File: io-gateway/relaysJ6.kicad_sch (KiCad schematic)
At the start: 24 parts, among them K1 2071556-2, K2 2071556-2, K3 2071556-2, K4 2071556-2, K5 2071556-2, K6 2071556-2, Q1 NTR4003NT1G, Q2 NTR4003NT1G, Q3 NTR4003NT1G, Q4 NTR4003NT1G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

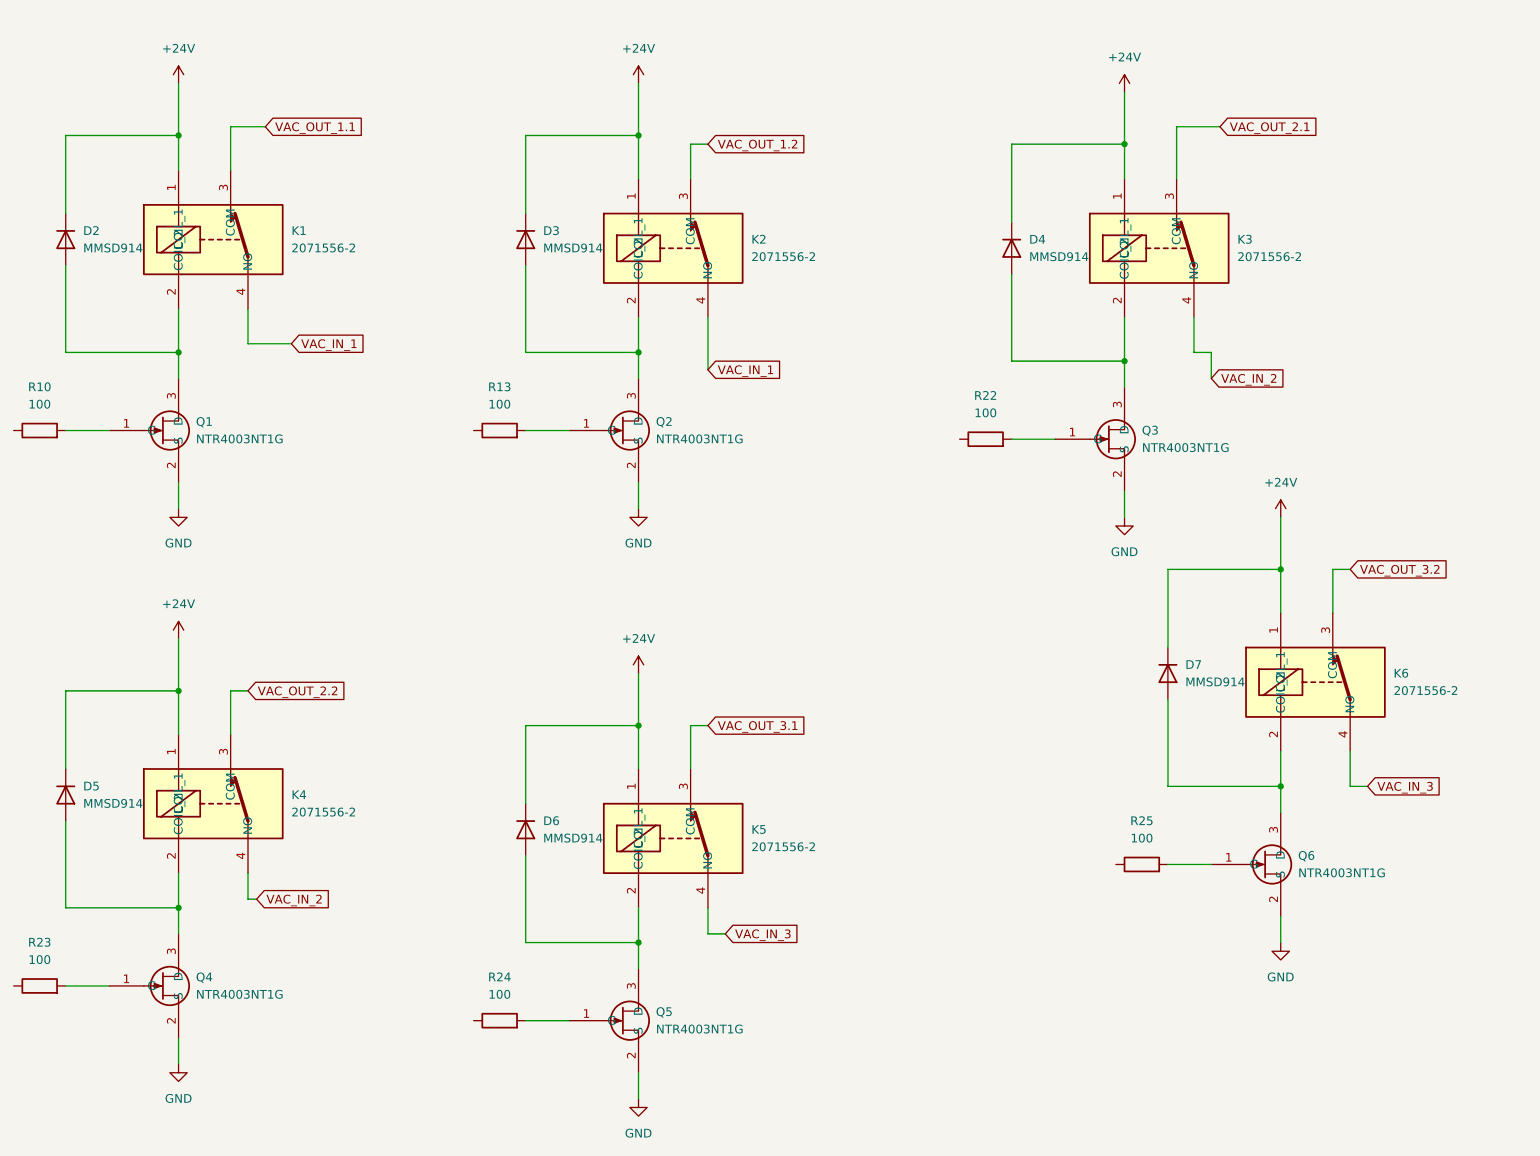
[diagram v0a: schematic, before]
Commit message: Place Relays
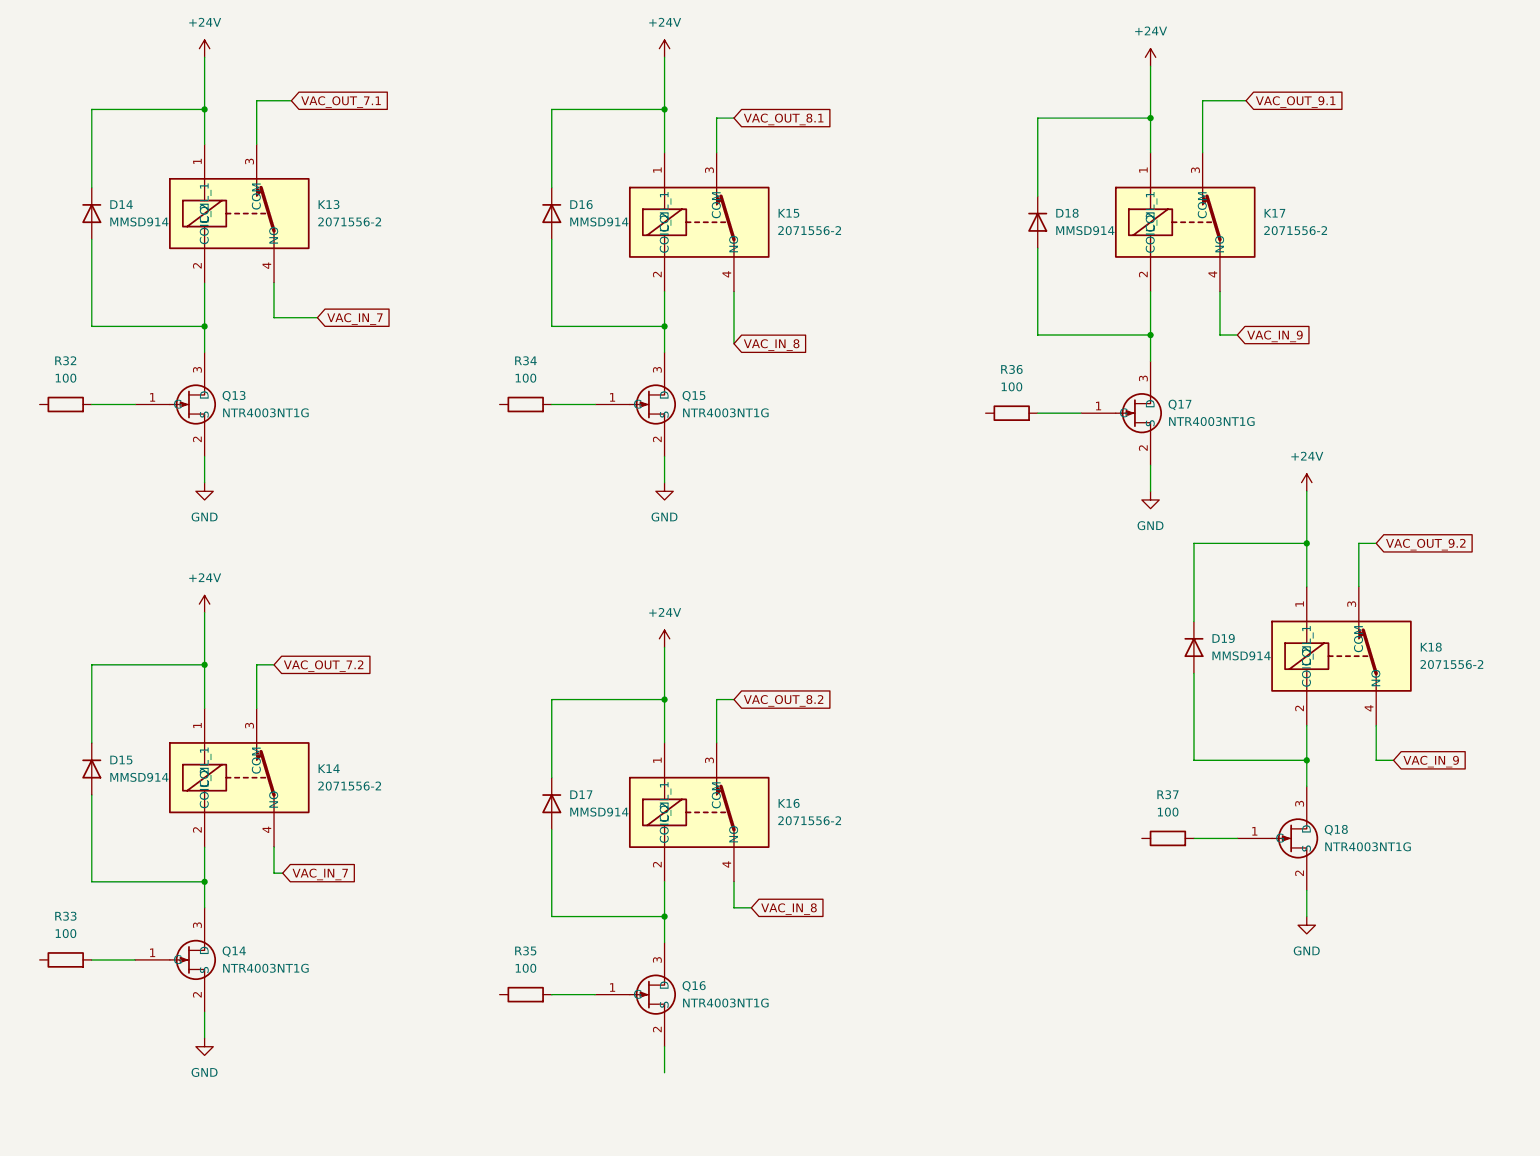
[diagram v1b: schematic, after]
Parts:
- removed D2, D3, D4, D5, D6, D7: MMSD914, Diode_SMD:D_SOD-123, symbol Diode:MMSD914
- removed K1, K2, K3, K4, K5, K6: 2071556-2, 20715562, symbol 2071556-2:2071556-2
- removed Q1, Q2, Q3, Q4, Q5, Q6: NTR4003NT1G, Package_TO_SOT_SMD:SOT-23-3, symbol NTR4003NT1G:NTR4003NT1G
- removed R10, R13, R22, R23, R24, R25: 100, Resistor_SMD:R_0603_1608Metric, symbol Device:R
- added D14, D15, D16, D17, D18, D19: MMSD914, Diode_SMD:D_SOD-123, symbol Diode:MMSD914
- added K13, K14, K15, K16, K17, K18: 2071556-2, 20715562, symbol 2071556-2:2071556-2
- added Q13, Q14, Q15, Q16, Q17, Q18: NTR4003NT1G, Package_TO_SOT_SMD:SOT-23-3, symbol NTR4003NT1G:NTR4003NT1G
- added R32, R33, R34, R35, R36, R37: 100, Resistor_SMD:R_0603_1608Metric, symbol Device:R
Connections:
- net +24V: now also D14.1 (K), D15.1 (K), D16.1 (K), D17.1 (K), D18.1 (K), D19.1 (K), K13.1 (COIL_1), K14.1 (COIL_1), K15.1 (COIL_1), K16.1 (COIL_1), K17.1 (COIL_1), K18.1 (COIL_1)
- net GND: now also Q13.2 (S), Q14.2 (S), Q15.2 (S), Q17.2 (S), Q18.2 (S)
- new net: D17.2 (A), K16.2 (COIL_2), Q16.3 (D)
- new net: Q15.1 (G), R34.2
- new net: D19.2 (A), K18.2 (COIL_2), Q18.3 (D)
- new net: D16.2 (A), K15.2 (COIL_2), Q15.3 (D)
- new net: D15.2 (A), K14.2 (COIL_2), Q14.3 (D)
- new net: Q16.1 (G), R35.2
- new net: Q17.1 (G), R36.2
- new net: D14.2 (A), K13.2 (COIL_2), Q13.3 (D)
- new net: Q18.1 (G), R37.2
- new net: Q13.1 (G), R32.2
- new net: Q14.1 (G), R33.2
- new net: D18.2 (A), K17.2 (COIL_2), Q17.3 (D)
- new net VAC_IN_7: K13.4 (NO), K14.4 (NO)
- new net VAC_IN_8: K15.4 (NO), K16.4 (NO)
- new net VAC_IN_9: K17.4 (NO), K18.4 (NO)
- new net VAC_OUT_7.1: K13.3 (COM)
- new net VAC_OUT_7.2: K14.3 (COM)
- new net VAC_OUT_8.1: K15.3 (COM)
- new net VAC_OUT_8.2: K16.3 (COM)
- new net VAC_OUT_9.1: K17.3 (COM)
- new net VAC_OUT_9.2: K18.3 (COM)

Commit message: update
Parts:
- removed D14, D15, D16, D17, D18, D19: MMSD914, Diode_SMD:D_SOD-123, symbol Diode:MMSD914
- removed K13, K14, K15, K16, K17, K18: 2071556-2, 20715562, symbol 2071556-2:2071556-2
- removed Q13, Q14, Q15, Q16, Q17, Q18: NTR4003NT1G, Package_TO_SOT_SMD:SOT-23-3, symbol NTR4003NT1G:NTR4003NT1G
- removed R32, R33, R34, R35, R36, R37: 100, Resistor_SMD:R_0603_1608Metric, symbol Device:R

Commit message: add RS485
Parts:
- added C1, C3: 100nF, Capacitor_SMD:C_0603_1608Metric, symbol Device:C
- added C2, C4: 10µF, Capacitor_SMD:C_0603_1608Metric, symbol Device:C
- added C5: 100µF, Capacitor_SMD:C_0603_1608Metric, symbol Device:C
- added D2, D3: MBR0520, Diode_SMD:D_SOD-123, symbol Diode:MBR0520
- added R1, R2: 4k7, Resistor_SMD:R_0201_0603Metric, symbol Device:R
- added TR1: Wuerth_750315371, Transformer_SMD:Transformer_Wuerth_750315371, symbol Transformer:Wuerth_750315371
- added U1: SN65LBC176QDR, Package_SO:SOIC-8_3.9x4.9mm_P1.27mm, symbol Interface_UART:SN65LBC176QDR
- added U2: TPS76350, Package_TO_SOT_SMD:SOT-23-5, symbol Regulator_Linear:TPS76350
- added U4: ISO7741, Package_SO:SOIC-16W_7.5x10.3mm_P1.27mm, symbol DigitalIsolator:ISO7741
- added U5: SN6501DBVR, Package_TO_SOT_SMD:SOT-23-5, symbol PowerManagement:SN6501DBVR
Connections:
- new net: R2.2, U4.7 (EN1)
- new net: TR1.1, U5.3 (D2)
- new net: TR1.3, U5.1 (D1)
- new net: C4.1, C5.1, D2.1 (K), TR1.4, U2.1 (VIN), U2.3 (EN)
- new net: D3.2 (A), TR1.5
- new net: D2.2 (A), TR1.6
- new net: U1.1 (R), U4.11 (IND)
- new net: U1.2 (~{RE}), U4.12 (OUTC)
- new net: U1.3 (DE), U4.14 (OUTA)
- new net: U1.4 (D), U4.13 (OUTB)
- new net: C4.2, C5.2, D3.1 (K)
- new net: C2.1, C3.1, R1.1, U2.5 (VOUT), U4.16 (VCC2)
- new net: R1.2, U4.10 (EN2)
- new net +5V: C1.1, R2.1, TR1.2, U1.8 (VCC), U4.1 (VCC1), U5.2 (VCC)
- new net GND: C1.2, U4.2 (GND1), U4.8 (GND1), U5.4 (GND), U5.5 (GND)
- new net GND2: C2.2, C3.2, U1.5 (GND), U2.2 (GND), U4.15 (GND2), U4.9 (GND2)
- new net RS485_DIR: U4.4 (INB)
- new net RS485_RxD: U4.6 (OUTD)
- new net RS485__TXD: U4.5 (INC)

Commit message: upd rs485
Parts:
- C5: value 100µF -> 100nF
- R1, R2: footprint Resistor_SMD:R_0201_0603Metric -> Resistor_SMD:R_0603_1608Metric
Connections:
- net GND2: now also C4.2, C5.2, D3.1 (K)
- net at U1.2 (~{RE}): now also U4.14 (OUTA); no longer U4.12 (OUTC)
- net at U1.3 (DE): now also U4.13 (OUTB); no longer U4.14 (OUTA)
- net at U1.4 (D): now also U4.12 (OUTC); no longer U4.13 (OUTB)
- net RS485_A: now reaches U1.6 (A)
- net RS485_B: now reaches U1.7 (B)
- net RS485_DIR renamed RS485_RTS
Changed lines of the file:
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@@
+	)
+	(junction
+		(at 123.19 87.63)
+		(diameter 0)
+		(color 0 0 0 0)
 	)
 	(junction
@@
 		(color 0 0 0 0)
 	)
+	(junction
+		(at 140.97 87.63)
+		(diameter 0)
+		(color 0 0 0 0)
+	)
+	(wire
+		(pts
+			(xy 123.19 87.63) (xy 140.97 87.63)
+		)
+		(stroke
+			(width 0)
+			(type default)
+		)
+	)
 	(wire
 		(pts
@@
 	(wire
 		(pts
-			(xy 196.85 113.03) (xy 196.85 115.57)
-		)
-		(stroke
-			(width 0)
-			(type default)
-		)
-	)
-	(wire
-		(pts
 			(xy 148.59 76.2) (xy 154.94 76.2)
 		)
@@
 	(wire
 		(pts
+			(xy 196.85 115.57) (xy 196.85 110.49)
+		)
+		(stroke
+			(width 0)
+			(type default)
+		)
+	)
+	(wire
+		(pts
 			(xy 91.44 81.28) (xy 91.44 87.63)
 		)
@@
 	(wire
 		(pts
+			(xy 190.5 118.11) (xy 198.12 118.11)
+		)
+		(stroke
+			(width 0)
+			(type default)
+		)
+	)
+	(wire
+		(pts
 			(xy 166.37 100.33) (xy 166.37 96.52)
 		)
@@
 	(wire
 		(pts
+			(xy 200.66 114.3) (xy 200.66 118.11)
+		)
+		(stroke
+			(width 0)
+			(type default)
+		)
+	)
+	(wire
+		(pts
 			(xy 193.04 100.33) (xy 195.58 100.33)
 		)
@@
 	(wire
 		(pts
-			(xy 196.85 115.57) (xy 190.5 115.57)
-		)
-		(stroke
-			(width 0)
-			(type default)
-		)
-	)
-	(wire
-		(pts
 			(xy 45.72 76.2) (xy 45.72 86.36)
 		)
@@
 	(wire
 		(pts
+			(xy 140.97 88.9) (xy 140.97 87.63)
+		)
+		(stroke
+			(width 0)
+			(type default)
+		)
+	)
+	(wire
+		(pts
 			(xy 73.66 78.74) (xy 67.31 78.74)
 		)
@@
 	(wire
 		(pts
-			(xy 193.04 113.03) (xy 190.5 113.03)
+			(xy 196.85 110.49) (xy 201.93 110.49)
+		)
+		(stroke
+			(width 0)
+			(type default)
+		)
+	)
+	(wire
+		(pts
+			(xy 190.5 113.03) (xy 194.31 113.03)
 		)
 		(stroke
@@
 	(wire
 		(pts
-			(xy 135.89 86.36) (xy 140.97 86.36)
+			(xy 217.17 120.65) (xy 224.79 120.65)
 		)
 		(stroke
@@
 	(wire
 		(pts
+			(xy 217.17 118.11) (xy 224.79 118.11)
+		)
+		(stroke
+			(width 0)
+			(type default)
+		)
+	)
+	(wire
+		(pts
 			(xy 190.5 76.2) (xy 167.64 76.2)
 		)
@@
 	(wire
 		(pts
+			(xy 198.12 118.11) (xy 198.12 113.03)
+		)
+		(stroke
+			(width 0)
+			(type default)
+		)
+	)
+	(wire
+		(pts
 			(xy 110.49 87.63) (xy 110.49 85.09)
 		)
@@
 	(wire
 		(pts
-			(xy 193.04 110.49) (xy 193.04 113.03)
-		)
-		(stroke
-			(width 0)
-			(type default)
-		)
-	)
-	(wire
-		(pts
 			(xy 73.66 83.82) (xy 67.31 83.82)
 		)
@@
 	(wire
 		(pts
+			(xy 198.12 113.03) (xy 201.93 113.03)
+		)
+		(stroke
+			(width 0)
+			(type default)
+		)
+	)
+	(wire
+		(pts
 			(xy 67.31 78.74) (xy 67.31 76.2)
 		)
@@
 	(wire
 		(pts
-			(xy 190.5 118.11) (xy 201.93 118.11)
+			(xy 194.31 113.03) (xy 194.31 114.3)
 		)
 		(stroke
@@
 	(wire
 		(pts
+			(xy 190.5 115.57) (xy 196.85 115.57)
+		)
+		(stroke
+			(width 0)
+			(type default)
+		)
+	)
+	(wire
+		(pts
+			(xy 200.66 118.11) (xy 201.93 118.11)
+		)
+		(stroke
+			(width 0)
+			(type default)
+		)
+	)
+	(wire
+		(pts
 			(xy 101.6 76.2) (xy 101.6 83.82)
 		)
@@
 	(wire
 		(pts
-			(xy 201.93 110.49) (xy 193.04 110.49)
-		)
-		(stroke
-			(width 0)
-			(type default)
-		)
-	)
-	(wire
-		(pts
 			(xy 123.19 76.2) (xy 130.81 76.2)
 		)
@@
 	(wire
 		(pts
+			(xy 194.31 114.3) (xy 200.66 114.3)
+		)
+		(stroke
+			(width 0)
+			(type default)
+		)
+	)
+	(wire
+		(pts
 			(xy 67.31 86.36) (xy 64.77 86.36)
 		)
@@
 	(wire
 		(pts
-			(xy 201.93 113.03) (xy 196.85 113.03)
+			(xy 140.97 87.63) (xy 140.97 86.36)
 		)
 		(stroke
@@
 		)
 	)
-	(hierarchical_label "RS485_DIR"
+	(hierarchical_label "RS485_B"
+		(shape bidirectional)
+		(at 224.79 118.11 0)
+		(effects
+			(font
+				(size 1.27 1.27)
+			)
+			(justify left)
+		)
+	)
+	(hierarchical_label "RS485_RTS"
 		(shape input)
 		(at 158.75 115.57 180)
@@
 			)
 			(justify right)
+		)
+	)
+	(hierarchical_label "RS485_A"
+		(shape bidirectional)
+		(at 224.79 120.65 0)
+		(effects
+			(font
+				(size 1.27 1.27)
+			)
+			(justify left)
 		)
 	)
@@
 			)
 		)
-		(property "Footprint" "Resistor_SMD:R_0201_0603Metric"
+		(property "Footprint" "Resistor_SMD:R_0603_1608Metric"
 			(at 146.812 101.6 90)
 			(effects
@@
 			)
 		)
-		(property "Footprint" "Resistor_SMD:R_0201_0603Metric"
+		(property "Footprint" "Resistor_SMD:R_0603_1608Metric"
 			(at 198.882 101.6 90)
 			(effects
@@
 			)
 		)
-		(property "Value" "100µF"
+		(property "Value" "100nF"
 			(at 127 82.5499 0)
 			(effects
@@
 	(symbol
 		(lib_id "power:GND2")
-		(at 135.89 86.36 0)
+		(at 140.97 88.9 0)
 		(unit 1)
 		(exclude_from_sim no)
@@
 		(fields_autoplaced yes)
 		(property "Reference" "#PWR056"
-			(at 135.89 92.71 0)
+			(at 140.97 95.25 0)
 			(effects
 				(font
@@
 		)
 		(property "Value" "GND2"
-			(at 135.89 91.44 0)
+			(at 140.97 93.98 0)
 			(effects
 				(font
@@
 		)
 		(property "Footprint" ""
-			(at 135.89 86.36 0)
+			(at 140.97 88.9 0)
 			(effects
 				(font
@@
 		)
 		(property "Datasheet" ""
-			(at 135.89 86.36 0)
+			(at 140.97 88.9 0)
 			(effects
 				(font
@@
 		)
 		(property "Description" "Power symbol creates a global label with name \"GND2\" , ground"
-			(at 135.89 86.36 0)
-			(effects
-				(font
+			(at 140.97 88.9 0)
+			(effects
+				(font

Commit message: connect rs485
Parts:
- added C6, C7: 10µF, Capacitor_SMD:C_0603_1608Metric, symbol Device:C
- added C8: 100nF, Capacitor_SMD:C_0603_1608Metric, symbol Device:C
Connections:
- net +5V: now also C6.1; no longer U1.8 (VCC)
- net GND: now also C6.2
- net GND2: now also C7.2, C8.2
- net at U1.2 (~{RE}): now also U1.3 (DE), U4.13 (OUTB); no longer U4.14 (OUTA)
- net at C2.1, C3.1, R1.1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: now also U1.8 (VCC), C7.1, C8.1
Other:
- moved on the sheet: C1

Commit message: upd
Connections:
- net RS485__TXD renamed RS485_TXD
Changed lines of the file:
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@@
 		)
 	)
-	(hierarchical_label "RS485__TXD"
+	(hierarchical_label "RS485_TXD"
 		(shape input)
 		(at 158.75 118.11 180)

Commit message: gen gerbers
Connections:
- net +5VP: now reaches C2.1, C3.1, C7.1, C8.1, R1.1, U1.8 (VCC), U2.5 (VOUT), U4.16 (VCC2)
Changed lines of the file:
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@@
+	)
+	(junction
+		(at 209.55 88.9)
+		(diameter 0)
+		(color 0 0 0 0)
 	)
 	(junction
@@
 		(pts
 			(xy 190.5 102.87) (xy 193.04 102.87)
+		)
+		(stroke
+			(width 0)
+			(type default)
+		)
+	)
+	(wire
+		(pts
+			(xy 209.55 86.36) (xy 209.55 88.9)
 		)
 		(stroke
@@
 					(unit 1)
 				)
+			)
+		)
+	)
+	(symbol
+		(lib_id "power:+5VP")
+		(at 209.55 86.36 0)
+		(unit 1)
+		(exclude_from_sim no)
+		(in_bom yes)
+		(on_board yes)
+		(dnp no)
+		(fields_autoplaced yes)
+		(property "Reference" "#PWR070"
+			(at 209.55 90.17 0)
+			(effects
+				(font
+					(size 1.27 1.27)
+				)
+				(hide yes)
+			)
+		)
+		(property "Value" "+5VP"
+			(at 209.55 81.28 0)
+			(effects
+				(font
+					(size 1.27 1.27)
+				)
+			)
+		)
+		(property "Footprint" ""
+			(at 209.55 86.36 0)
+			(effects
+				(font
+					(size 1.27 1.27)
+				)
+				(hide yes)
+			)
+		)
+		(property "Datasheet" ""
+			(at 209.55 86.36 0)
+			(effects
+				(font
+					(size 1.27 1.27)
+				)
+				(hide yes)
+			)
+		)
+		(property "Description" "Power symbol creates a global label with name \"+5VP\""
+			(at 209.55 86.36 0)
+			(effects
+				(font
+					(size 1.27 1.27)
+				)
+				(hide yes)
+			)
+		)
+		(pin "1"
+		)
+		(instances
+			(project ""
+				(path "/2cb6f94b-272a-4ed7-b08d-c3630bda6156/1308d9d5-cfd2-45e8-87f7-78f75fc0ae30"
+					(reference "#PWR070")
+					(unit 1)
+				)
